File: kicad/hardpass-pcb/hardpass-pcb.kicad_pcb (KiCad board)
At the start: 2 copper layers, 80 x 65 mm, 57 parts, among them IC1 APX803, P1 Pi_Zero, P2 OLED_I2C, P3 Pi_Zero, SW1 1, SW10 C/UP, SW11 0/OK, SW12 OK/DN, SW2 2, SW3 3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

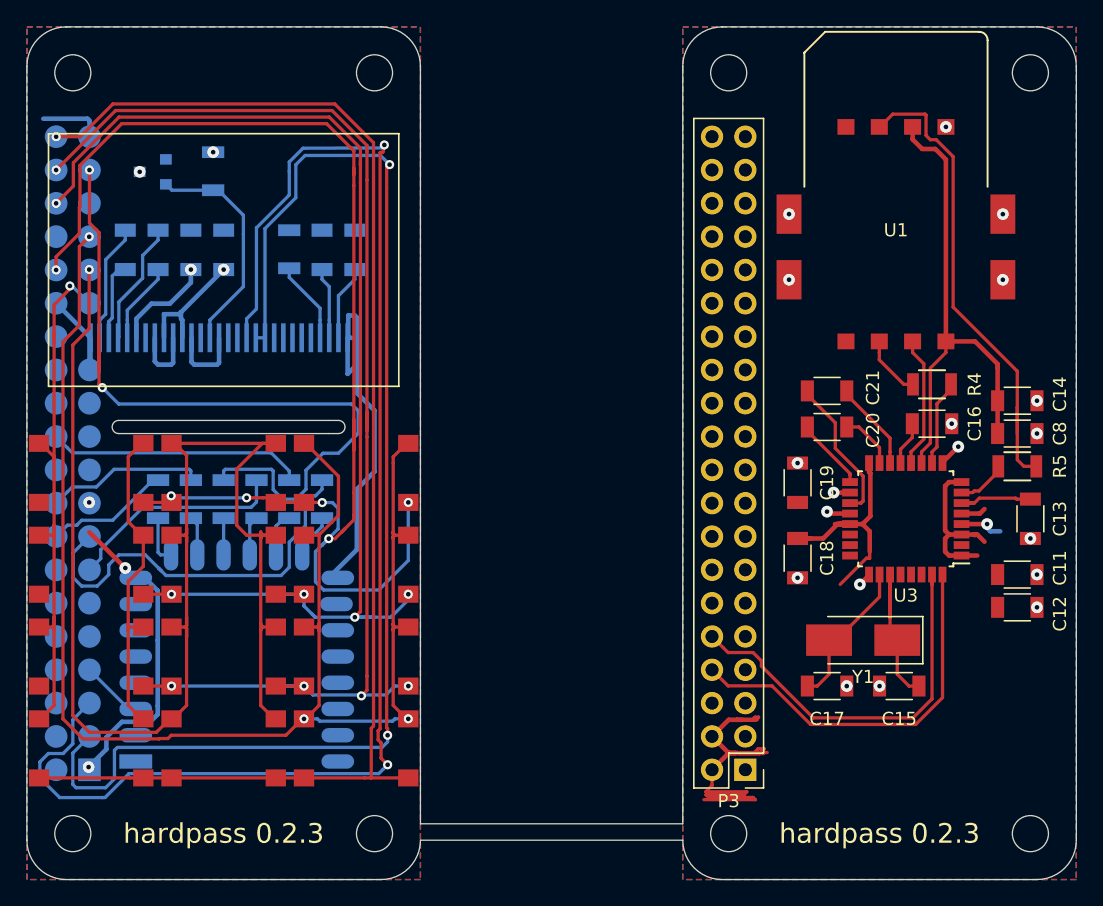
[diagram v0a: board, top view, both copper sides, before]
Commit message: seperate hardpass-frontend from hardpass-sci, II
(I) was sci
(II) is frontend

also general cleanup and version bump to 0.2.5
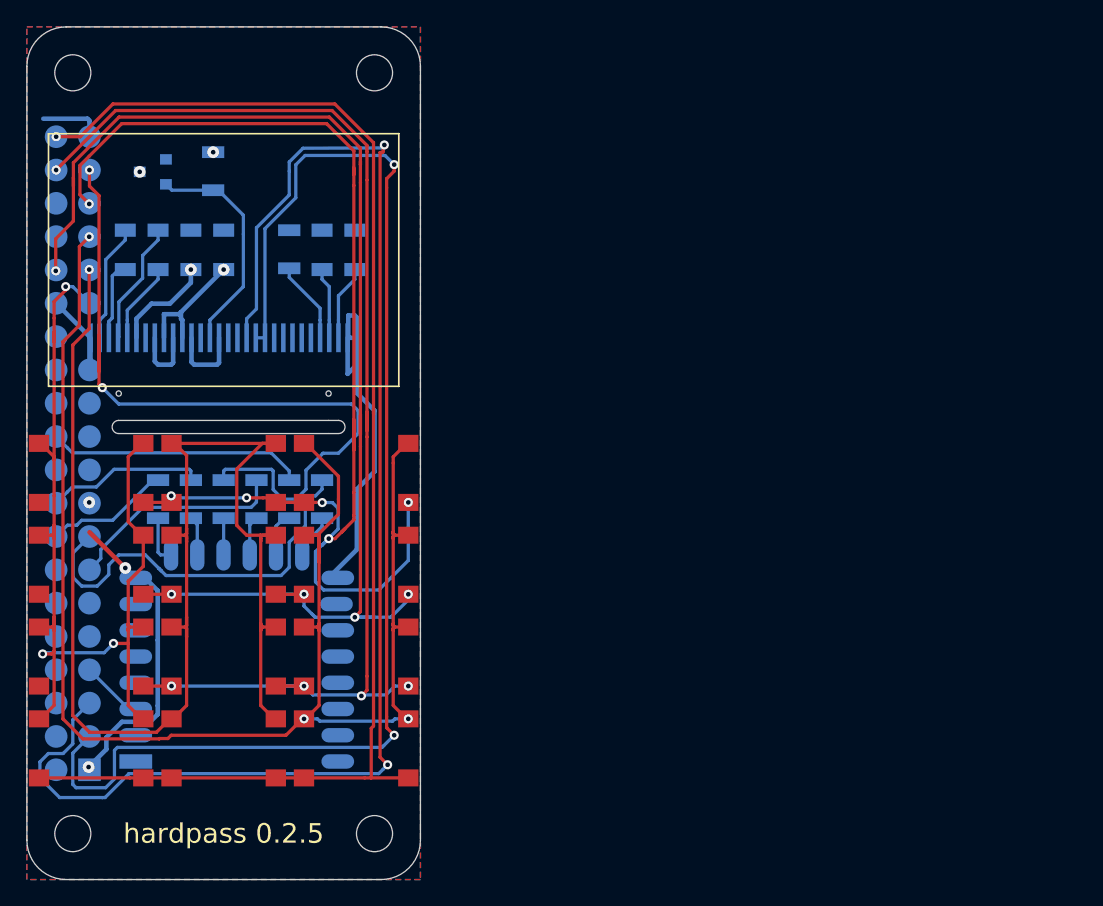
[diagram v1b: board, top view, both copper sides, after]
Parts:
- removed the ? at (53.5, 61.5)
- removed the ? at (76.5, 61.5)
- removed the ? at (76.5, 3.50)
- removed the ? at (53.5, 3.50)
- removed C11, C19: 10µF, Capacitors_SMD:C_1206
- removed C12, C18: 100nF, Capacitors_SMD:C_1206
- removed C13: 22nF, Capacitors_SMD:C_1206
- removed C14: 100pF, Capacitors_SMD:C_1206
- removed C15, C17: 22pF, Capacitors_SMD:C_1206
- removed C16, C20, C21, C8: 220nF, Capacitors_SMD:C_1206
- removed P1: Pi_Zero, hardpass:Pin_Header_Mirrored-NoHoles_centered_2x20
- removed P3: Pi_Zero, hardpass:Pin_Header_Straight_2x20_Pitch2.54mm_centered
- removed R4: 100, Resistors_SMD:R_1206
- removed R5: 180, Resistors_SMD:R_1206
- removed REF**: Symbol_GNU-Logo_MaskTop, hardpass:Symbol_GNU-Logo_MaskTop
- removed U1: ISO7816, hardpass:CAF99-08153-S132
- removed U3: TDA8029, Housings_QFP:LQFP-32_7x7mm_Pitch0.8mm
- removed Y1: 14.745MHz, Crystals:Crystal_SMD_5032-2pin_5.0x3.2mm_HandSoldering
- added J1: Raspberry_Pi_2_3, hardpass:Pin_Header_Mirrored-NoHoles_centered_2x20, B.Cu at (3.50, 32.5)
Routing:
- net +5V: track 73.8 -> 0.00 mm
- net Net-(C14-Pad2): track 38.0 -> 0.00 mm
- net Net-(R5-Pad1): track 37.1 -> 0.00 mm
- net CARD_TX: track 30.4 -> 0.00 mm
- net CARD_RX: track 29.5 -> 0.00 mm
- net Net-(C15-Pad2): track 13.2 -> 0.00 mm
- net Net-(C17-Pad2): track 11.5 -> 0.00 mm
- net Net-(C21-Pad1): track 11.2 -> 0.00 mm
- net Net-(U1-Pad2): track 10.0 -> 0.00 mm
- net GND: track 61.8 -> 52.9 mm, vias 20 -> 0
- net COL_1: track 67.7 -> 75.6 mm, vias 1 -> 3
- net Net-(C21-Pad2): track 6.87 -> 0.00 mm
- net Net-(R4-Pad2): track 6.60 -> 0.00 mm
- net Net-(C13-Pad1): track 6.29 -> 0.00 mm
- net ROW_2: track 92.1 -> 97.7 mm
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- removed copper zone on F.Cu, net +5V
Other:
- board size 80 x 65 mm -> 30 x 65 mm
- board text added: "hardpass 0.2.5"
- board text removed: "hardpass 0.2.3"

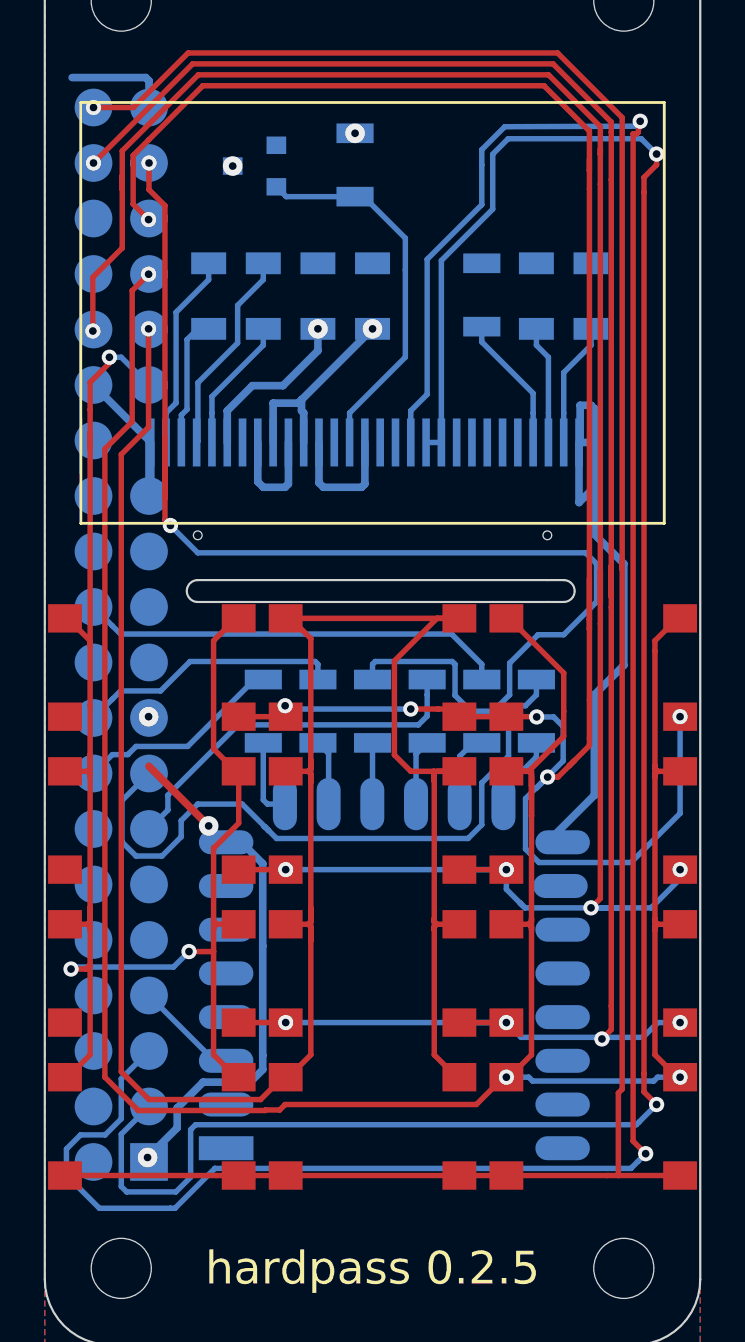
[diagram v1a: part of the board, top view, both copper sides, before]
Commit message: redesign frontend with 5.2mm tact switches
reason being, those are flat enough so they don't protrude above the
oled. I'm thinking about putting a lasercut sheet of plexiglass as a
protecting case in front
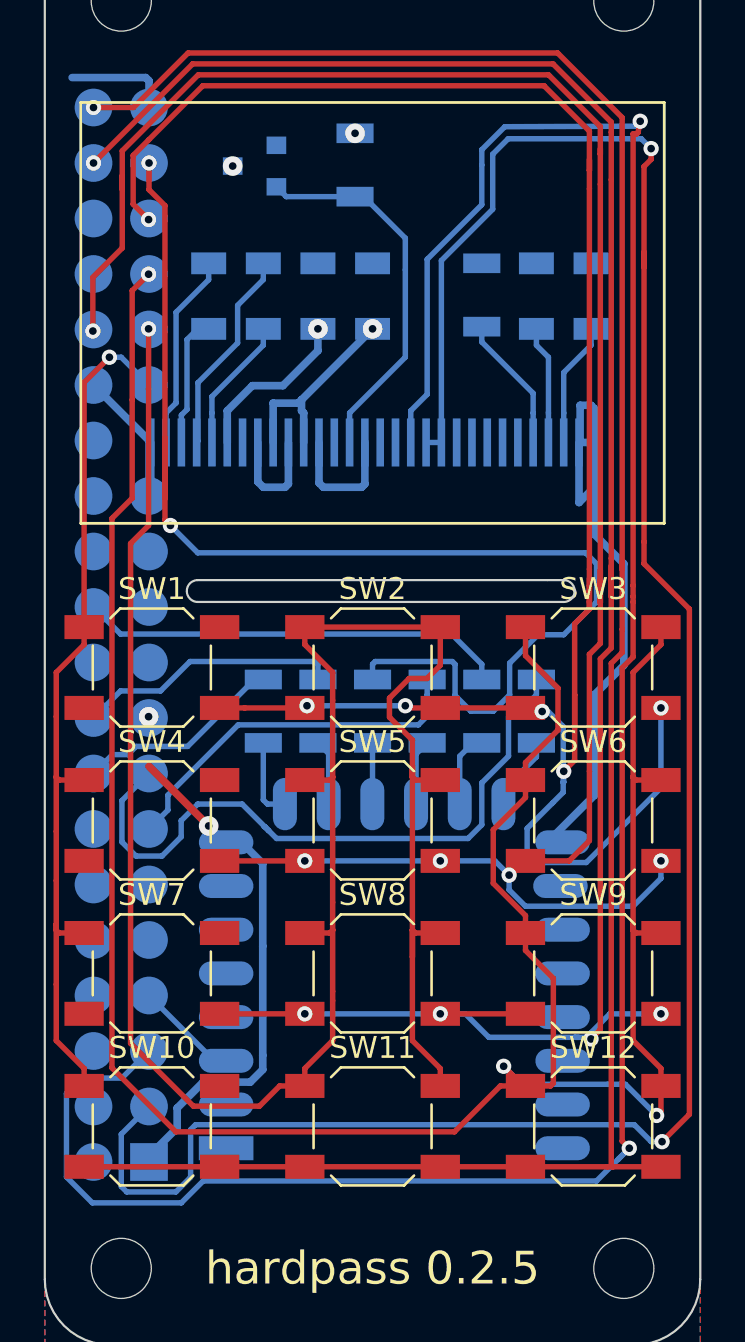
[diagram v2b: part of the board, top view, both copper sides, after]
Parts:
- P2: footprint adafruit-oled:UG-2864HSWEG01_0.96IN_WRAPAROUND -> hardpass:UG-2864HSWEG01_0.96IN_WRAPAROUND
- SW1, SW10, SW11, SW12, SW2, SW3, SW4, SW5, SW6, SW7, SW8, SW9: footprint hardpass:SW_SPST_PTS645_nosilk -> Buttons_Switches_SMD:SW_SPST_SKQG
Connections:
- J1 pad 6: GND -> (no net)
- J1 pad 9: GND -> (no net)
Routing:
- net COL_1: track 75.6 -> 40.2 mm, vias 3 -> 1
- net COL_2: track 107.1 -> 102.3 mm
- net OLED_SDA: track 98.6 -> 102.1 mm
- net ROW_3: track 93.4 -> 95.9 mm
- net ROW_1: track 95.9 -> 93.8 mm
- net ROW_4: track 103.6 -> 101.5 mm
- net COL_3: track 120.3 -> 119.0 mm
- net ROW_2: track 97.7 -> 96.5 mm
- net +3V3: vias 7 -> 6

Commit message: cleanup on the frontend-pcb
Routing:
- net COL_1: track 40.2 -> 82.0 mm, vias 1 -> 3
- net OLED_SCL: track 106.4 -> 99.2 mm, vias 2 -> 4
- net +3V3: track 42.4 -> 39.9 mm
- net ROW_1: track 93.8 -> 94.9 mm
- net OLED_SDA: track 102.1 -> 102.9 mm
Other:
- board text added: "Shutdown Footprint!"

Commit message: cleanup frontend-pcb some more, shutdown-button-note
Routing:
- net SHUTDOWN: track 0.00 -> 36.1 mm, vias 0 -> 2

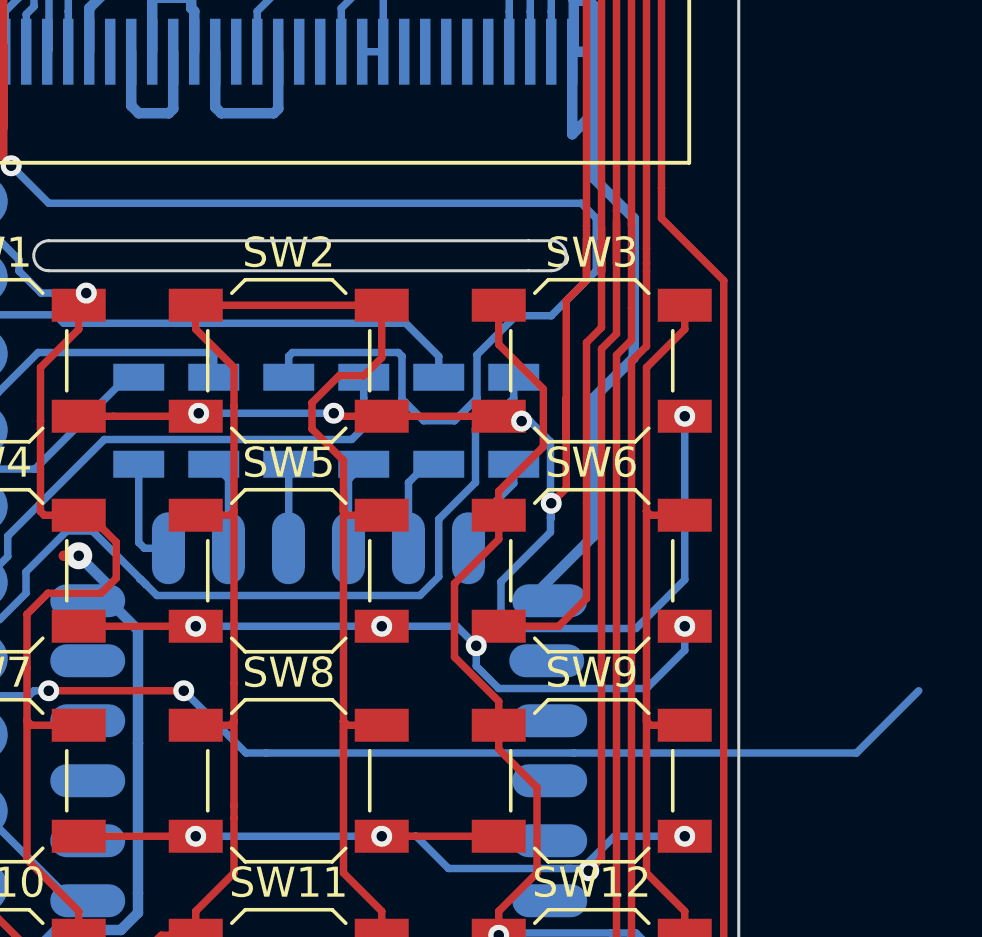
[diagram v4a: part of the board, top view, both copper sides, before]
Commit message: more shutdown-button routing
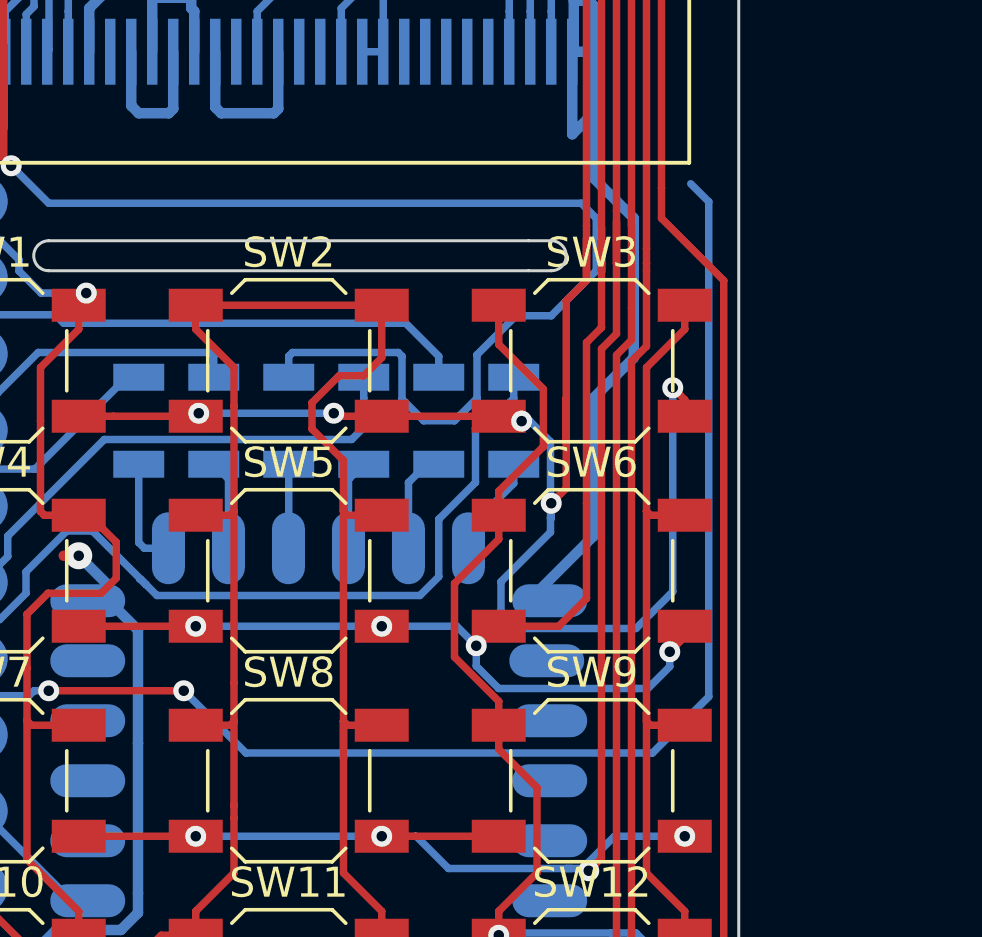
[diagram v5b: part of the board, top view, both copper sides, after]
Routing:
- net SHUTDOWN: track 36.1 -> 46.3 mm
- net ROW_1: track 94.9 -> 96.8 mm
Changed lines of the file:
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@@
     (links 98)
     (no_connects 0)
-    (area -4.40411 -1.5255 30.050001 66.22418)
+    (area -0.050001 -0.050001 30.050001 65.050001)
     (thickness 1.6)
-    (drawings 16)
-    (tracks 580)
+    (drawings 28)
+    (tracks 586)
     (zones 0)
     (modules 34)
@@
     )
   )
-  (gr_text "Shutdown\nFootprint!" (at 41.75 45) (layer Dwgs.User)
+  (gr_circle (center 28.4 28) (end 27.6 28) (layer Dwgs.User) (width 0.2))
+  (gr_line (start 42.6 24) (end 41.6 24) (layer Dwgs.User) (width 0.2))
+  (gr_line (start 43.4 24.8) (end 43.4 29) (layer Dwgs.User) (width 0.2))
+  (gr_arc (start 42.6 29) (end 43.4 29) (angle 90) (layer Dwgs.User) (width 0.2))
+  (gr_arc (start 42.6 24.8) (end 42.6 24) (angle 90) (layer Dwgs.User) (width 0.2))
+  (gr_line (start 32.2 24) (end 41.8 24) (layer Dwgs.User) (width 0.2))
+  (gr_line (start 31.2 25) (end 31.2 25.2) (layer Dwgs.User) (width 0.2))
+  (gr_arc (start 32.2 25) (end 31.2 25) (angle 90) (layer Dwgs.User) (width 0.2))
+  (gr_arc (start 30.2 25.2) (end 31.2 25.2) (angle 90) (layer Dwgs.User) (width 0.2))
+  (gr_line (start 28.4 26.2) (end 30.3 26.2) (layer Dwgs.User) (width 0.2))
+  (gr_line (start 28.3 29.8) (end 42.6 29.8) (layer Dwgs.User) (width 0.2))
+  (gr_arc (start 28.3 28) (end 28.3 29.8) (angle 183.5763344) (layer Dwgs.User) (width 0.2))
+  (gr_text "Shutdown\nFootprint!" (at 37.2 27) (layer Dwgs.User)
     (effects (font (size 1.5 1.5) (thickness 0.3)))
   )
@@
   (segment (start 9 52) (end 7.7597 52) (width 0.25) (layer B.Cu) (net 11))
   (segment (start 7.7597 52) (end 4.7697 49.01) (width 0.25) (layer B.Cu) (net 11))
-  (segment (start 33.92501 47.07499) (end 36 45) (width 0.25) (layer B.Cu) (net 12))
-  (segment (start 24.5 47.07499) (end 33.92501 47.07499) (width 0.25) (layer B.Cu) (net 12))
-  (segment (start 14.25 47.07499) (end 24.5 47.07499) (width 0.25) (layer B.Cu) (net 12))
+  (segment (start 29 28.7) (end 28.4 28.1) (width 0.25) (layer B.Cu) (net 12))
+  (segment (start 27.8 46.4) (end 27.12501 47.07499) (width 0.25) (layer B.Cu) (net 12))
+  (segment (start 27.8 46.4) (end 29 45.2) (width 0.25) (layer B.Cu) (net 12))
+  (segment (start 29 45.2) (end 29 28.7) (width 0.25) (layer B.Cu) (net 12))
+  (segment (start 27.12501 47.07499) (end 13.57499 47.07499) (width 0.25) (layer B.Cu) (net 12))
+  (segment (start 13.57499 47.07499) (end 11.5 45) (width 0.25) (layer B.Cu) (net 12))
   (segment (start 11.5 45) (end 7 45) (width 0.25) (layer F.Cu) (net 12))
-  (segment (start 11.5 45) (end 13.57499 47.07499) (width 0.25) (layer B.Cu) (net 12))
-  (segment (start 13.57499 47.07499) (end 14.25 47.07499) (width 0.25) (layer B.Cu) (net 12))
   (via (at 11.5 45) (size 0.7) (drill 0.35) (layers F.Cu B.Cu) (net 12))
   (segment (start 3.468301 45.168601) (end 5.5 45.168601) (width 0.25) (layer B.Cu) (net 12))
@@
   (segment (start 4.75 18.5103) (end 4.7697 18.53) (width 0.25) (layer B.Cu) (net 19))
   (segment (start 4.75 18.5) (end 4.75 18.5103) (width 0.25) (layer B.Cu) (net 19))
-  (segment (start 28.2 39.25) (end 28.2 35.85) (width 0.25) (layer B.Cu) (net 20))
+  (segment (start 26.57499 42.92501) (end 27.7 41.8) (width 0.25) (layer B.Cu) (net 20))
+  (segment (start 27.8 34.9) (end 27.8 41.7) (width 0.25) (layer B.Cu) (net 20))
+  (segment (start 27.8 41.7) (end 27.7 41.8) (width 0.25) (layer B.Cu) (net 20))
+  (segment (start 28.2 35.85) (end 28.2 35.3) (width 0.25) (layer F.Cu) (net 20))
+  (segment (start 28.2 35.3) (end 27.8 34.9) (width 0.25) (layer F.Cu) (net 20))
+  (via (at 27.8 34.9) (size 0.7) (drill 0.35) (layers F.Cu B.Cu) (net 20))
   (segment (start 23.725001 39.25) (end 23.725001 39.714318) (width 0.25) (layer B.Cu) (net 20))
   (segment (start 23.725001 39.714318) (end 22.07499 41.364329) (width 0.25) (layer B.Cu) (net 20))
@@
   (segment (start 22.07499 42.383151) (end 22.616849 42.92501) (width 0.25) (layer B.Cu) (net 20))
   (segment (start 22.616849 42.92501) (end 26.57499 42.92501) (width 0.25) (layer B.Cu) (net 20))
-  (segment (start 26.57499 42.92501) (end 28.2 41.3) (width 0.25) (layer B.Cu) (net 20))
-  (segment (start 28.2 41.3) (end 28.2 39.25) (width 0.25) (layer B.Cu) (net 20))
   (segment (start 16.5 35.75) (end 12 35.75) (width 0.25) (layer B.Cu) (net 20))
   (via (at 12 35.75) (size 0.7) (drill 0.35) (layers F.Cu B.Cu) (net 20))
@@
   (segment (start 23.037655 36.012653) (end 22.762653 36.012653) (width 0.25) (layer B.Cu) (net 20))
   (via (at 22.762653 36.012653) (size 0.7) (drill 0.35) (layers F.Cu B.Cu) (net 20))
-  (via (at 28.2 35.85) (size 0.7) (drill 0.35) (layers F.Cu B.Cu) (net 20))
   (segment (start 18.1 35.85) (end 22 35.85) (width 0.25) (layer F.Cu) (net 20))
   (segment (start 8 35.85) (end 9.15 35.85) (width 0.25) (layer F.Cu) (net 20))
@@
   (segment (start 22 53.15) (end 21.9 53.15) (width 0.25) (layer F.Cu) (net 21))
   (via (at 4.75 16) (size 0.7) (drill 0.35) (layers F.Cu B.Cu) (net 21))
+  (segment (start 27.7 44.194974) (end 26.969964 44.92501) (width 0.25) (layer B.Cu) (net 22))
+  (segment (start 26.6 44.92501) (end 22 44.92501) (width 0.25) (layer B.Cu) (net 22))
+  (segment (start 27.7 43.7) (end 27.7 44.194974) (width 0.25) (layer B.Cu) (net 22))
+  (segment (start 26.969964 44.92501) (end 26.6 44.92501) (width 0.25) (layer B.Cu) (net 22))
+  (segment (start 28.2 42.85) (end 28.2 43.2) (width 0.25) (layer F.Cu) (net 22))
+  (via (at 27.7 43.7) (size 0.7) (drill 0.35) (layers F.Cu B.Cu) (net 22))
+  (segment (start 28.2 43.2) (end 27.7 43.7) (width 0.25) (layer F.Cu) (net 22))
   (segment (start 24.924959 41.925041) (end 24 42.85) (width 0.25) (layer F.Cu) (net 22))
   (segment (start 24.924959 38.75) (end 24.924959 40) (width 0.25) (layer F.Cu) (net 22))
   (segment (start 24 42.85) (end 22 42.85) (width 0.25) (layer F.Cu) (net 22))
   (segment (start 24.924959 40) (end 24.924959 41.925041) (width 0.25) (layer F.Cu) (net 22))
-  (segment (start 26.92499 44.92501) (end 22 44.92501) (width 0.25) (layer B.Cu) (net 22))
   (segment (start 21.25 43.5) (end 21.25 44.17501) (width 0.25) (layer B.Cu) (net 22))
   (segment (start 21.25 44.17501) (end 22 44.92501) (width 0.25) (layer B.Cu) (net 22))
@@
   (segment (start 25.424949 30) (end 25.424949 30.5) (width 0.25) (layer F.Cu) (net 22))
   (segment (start 25.424949 29.546309) (end 25.424949 30) (width 0.25) (layer F.Cu) (net 22))
-  (segment (start 28.2 42.85) (end 28.2 43.65) (width 0.25) (layer B.Cu) (net 22))
-  (segment (start 28.2 43.65) (end 26.92499 44.92501) (width 0.25) (layer B.Cu) (net 22))
-  (via (at 28.2 42.85) (size 0.7) (drill 0.35) (layers F.Cu B.Cu) (net 22))
   (segment (start 11.9 42.85) (end 18.1 42.85) (width 0.25) (layer B.Cu) (net 22))
   (via (at 18.1 42.85) (size 0.7) (drill 0.35) (layers F.Cu B.Cu) (net 22))
